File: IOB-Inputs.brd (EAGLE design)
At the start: 20.3 x 50.8 mm, 34 parts, among them J1 RJ12/6, Q0 P-FET, Q1 P-FET, Q2 P-FET, Q3 P-FET

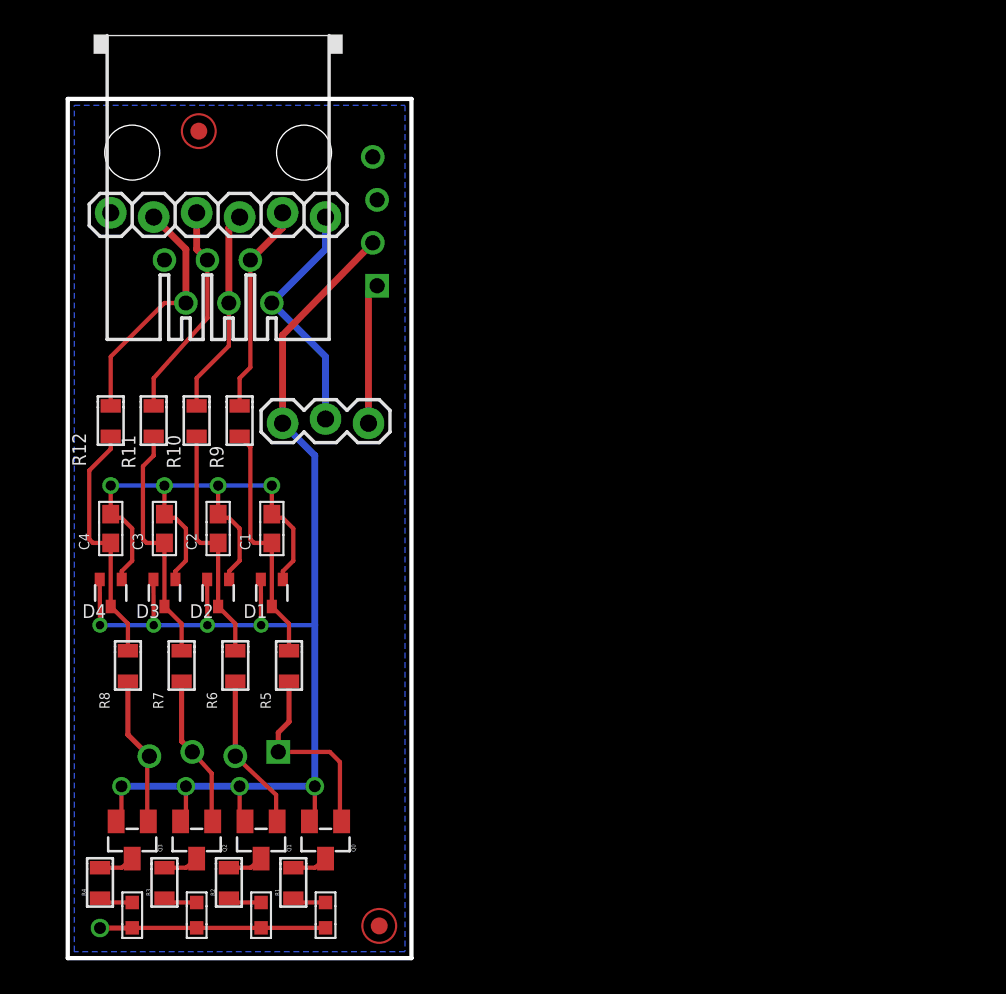
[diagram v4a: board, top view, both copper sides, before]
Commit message: new IOB design
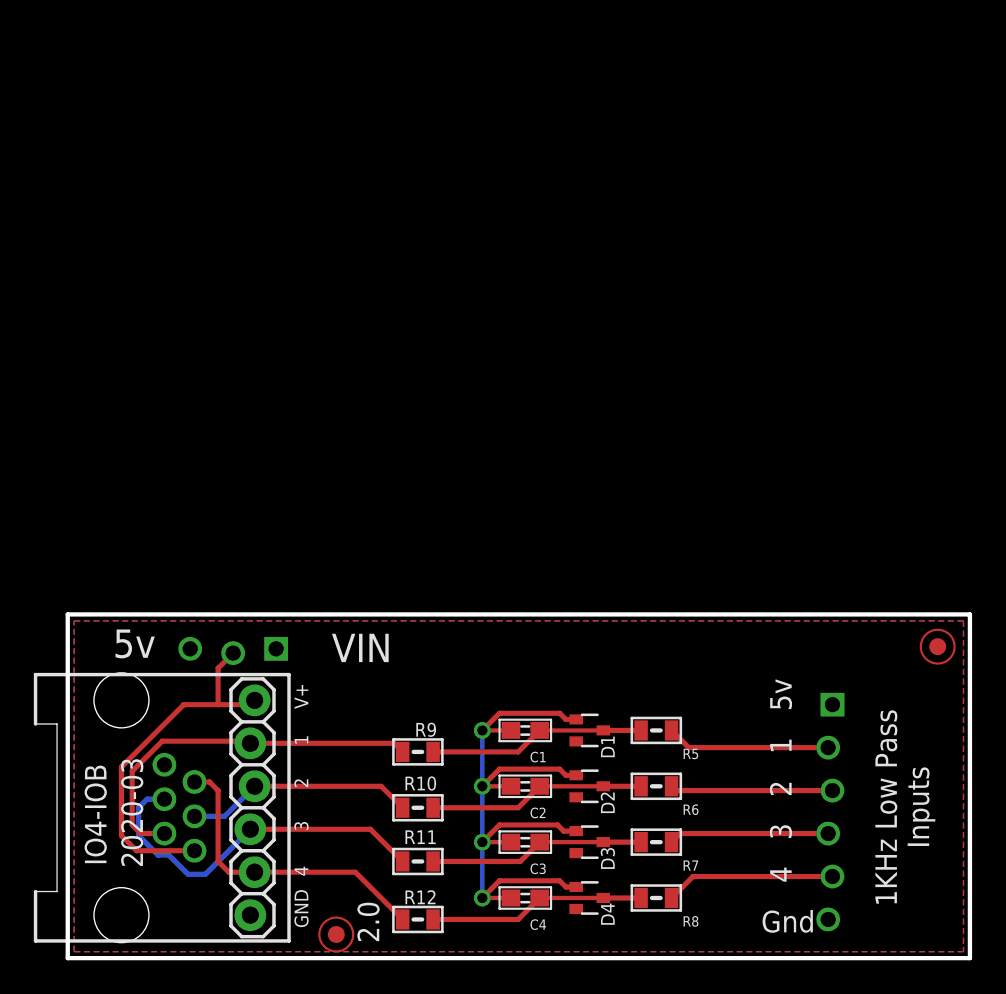
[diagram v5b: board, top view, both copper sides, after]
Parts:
- removed CON1: (no value), SPCoast:1X06_LOCK
- removed LED1, LED2, LED3, LED4: Y, SPCoast:0603-LED
- removed Q0, Q1, Q2, Q3: P-FET, SPCoast:SOT23
- removed R1, R2, R3, R4: 2K0, SPCoast:0805-RES
- removed VIN: (no value), SPCoast:1X03
- J1: device SPCoast:RJ25-PANEL -> SPCoast:RJ24-INVERTED-PINS
- moved IOB 50.8 mm to (0.00, 0.00), turned to 0 degrees
- moved FID1 48.2 mm to (15.9, 1.40), turned to 0 degrees
- moved J1 38.8 mm to (6.99, 8.89), turned to 90 degrees
- moved FID2 36.9 mm to (51.4, 18.4), turned to 0 degrees
- moved R12 34.6 mm to (20.7, 2.29), turned to 180 degrees
- moved R8 34.1 mm to (34.8, 3.56), turned to 180 degrees
- moved D4 33.6 mm to (30.9, 3.56), turned to 270 degrees
- moved C4 32.8 mm to (27.1, 3.56), turned to 180 degrees
- moved R11 30.4 mm to (20.7, 5.71), turned to 180 degrees
- moved R7 29.9 mm to (34.8, 6.86), turned to 180 degrees
- moved D3 29.1 mm to (30.9, 6.86), turned to 270 degrees
- moved C3 28.3 mm to (27.1, 6.86), turned to 180 degrees
- moved R10 26.3 mm to (20.7, 8.89), turned to 180 degrees
- moved R6 25.9 mm to (34.8, 10.2), turned to 180 degrees
- moved D2 24.8 mm to (30.9, 10.2), turned to 270 degrees
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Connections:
- removed net N$1: CON1.1, J1.1, VIN.2
- removed net N$11: Q0.3, R1.2
- removed net N$2: LED1.A, R1.1
- removed net N$3: LED2.A, R2.1
- removed net N$30: Q1.3, R2.2
- removed net N$31: Q2.3, R3.2
- removed net N$32: Q3.3, R4.2
- removed net N$4: LED3.A, R3.1
- removed net N$5: LED4.A, R4.1
- new net VOUT: IOB.VOUT, J1.1, J1.1@1
- net !IO1: now also J1.2@1; no longer CON1.2
- net !IO2: now also J1.3@1; no longer CON1.3
- net !IO3: now also J1.4@1; no longer CON1.4
- net !IO4: now also J1.5@1; no longer CON1.5
- net GND: now also IOB.G@3, J1.6@1; no longer CON1.6, IOB.G@1, IOB.G@2, LED1.C, LED2.C, LED3.C, LED4.C
- net P1: no longer Q0.1
- net P2: no longer Q1.1
- net P3: no longer Q2.1
- net P4: no longer Q3.1
- net VCC: now also IOB.V5@1; no longer Q0.2, Q1.2, Q2.2, Q3.2, VIN.1
- net VCCIO: no longer VIN.3
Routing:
- net VCC: track 79.2 -> 0.00 mm, vias 8 -> 0
- net VOUT: track 0.00 -> 21.7 mm
- net N$1: track 14.6 -> 0.00 mm
- net !IO1: track 12.5 -> 22.3 mm
- net !IO3: track 12.9 -> 21.8 mm
- net VCCIO: track 8.38 -> 0.00 mm
- net GND: track 49.2 -> 41.2 mm, vias 5 -> 4
- net !IO4: track 14.5 -> 18.1 mm
- net P1: track 12.0 -> 9.68 mm
- net N$31: track 2.11 -> 0.00 mm
- net N$32: track 2.11 -> 0.00 mm
- net N$30: track 2.11 -> 0.00 mm
- net N$11: track 2.11 -> 0.00 mm
- net N$4: track 2.01 -> 0.00 mm
- net N$5: track 2.01 -> 0.00 mm
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- added copper zone on layer 1, net VCC
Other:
- board size 20.3 x 50.8 mm -> 53.3 x 20.3 mm
- board text added: "1KHz Low Pass"
- board text added: "2.0"
- board text added: "2020-03"
- board text removed: "1"
- board text removed: "1.4"
- board text removed: "2"
- board text removed: "3"
- board text removed: "4"
- board text removed: "5v"
- board text removed: "9v"
- board text removed: "IO4 Power"
- board text removed: "IOB to IO4 Interface"
- board text removed: "Made in the PCR, Coast Div, NMRA"
- board text removed: "Model Railroading is Fun!"
- board text removed: "Q0"
- board text removed: "Q1"
- board text removed: "Q2"
- board text removed: "Q3"
- board text removed: "R1"
- board text removed: "R2"
- board text removed: "R3"
- board text removed: "R4"

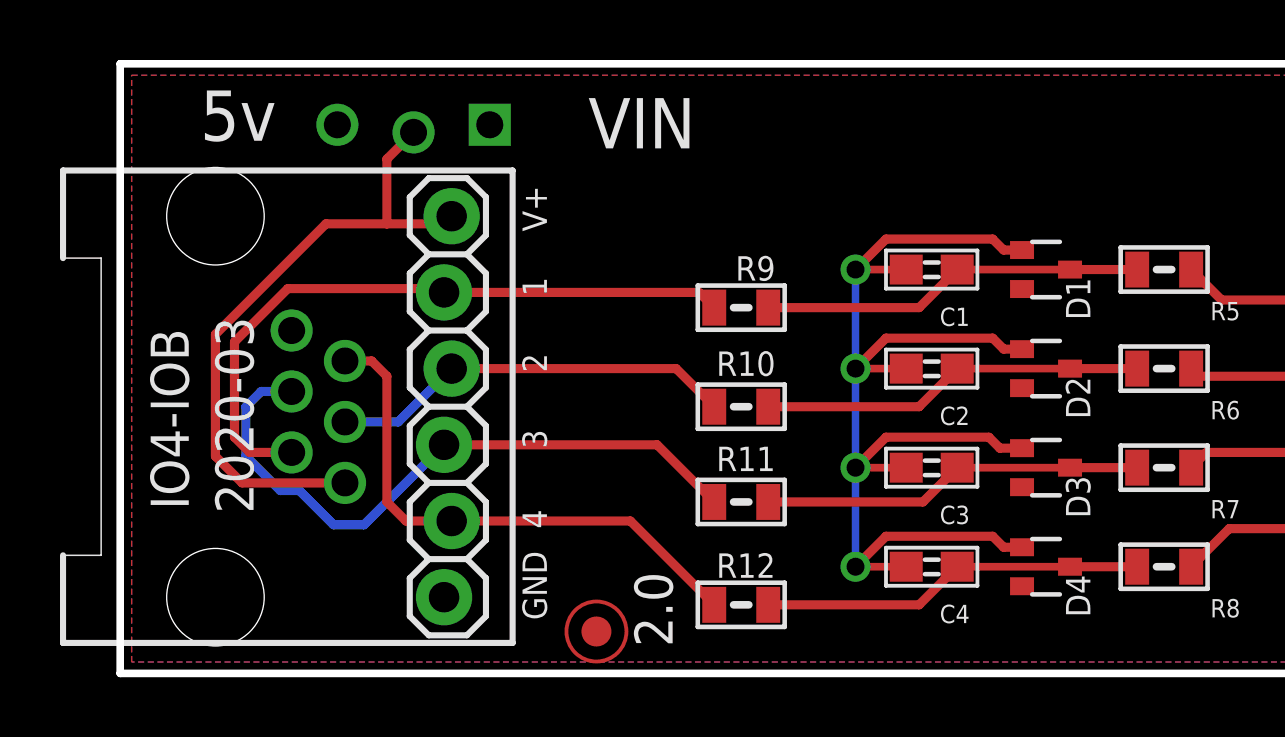
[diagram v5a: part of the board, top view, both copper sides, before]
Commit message: fixed SPCoast.lbr diode orientation
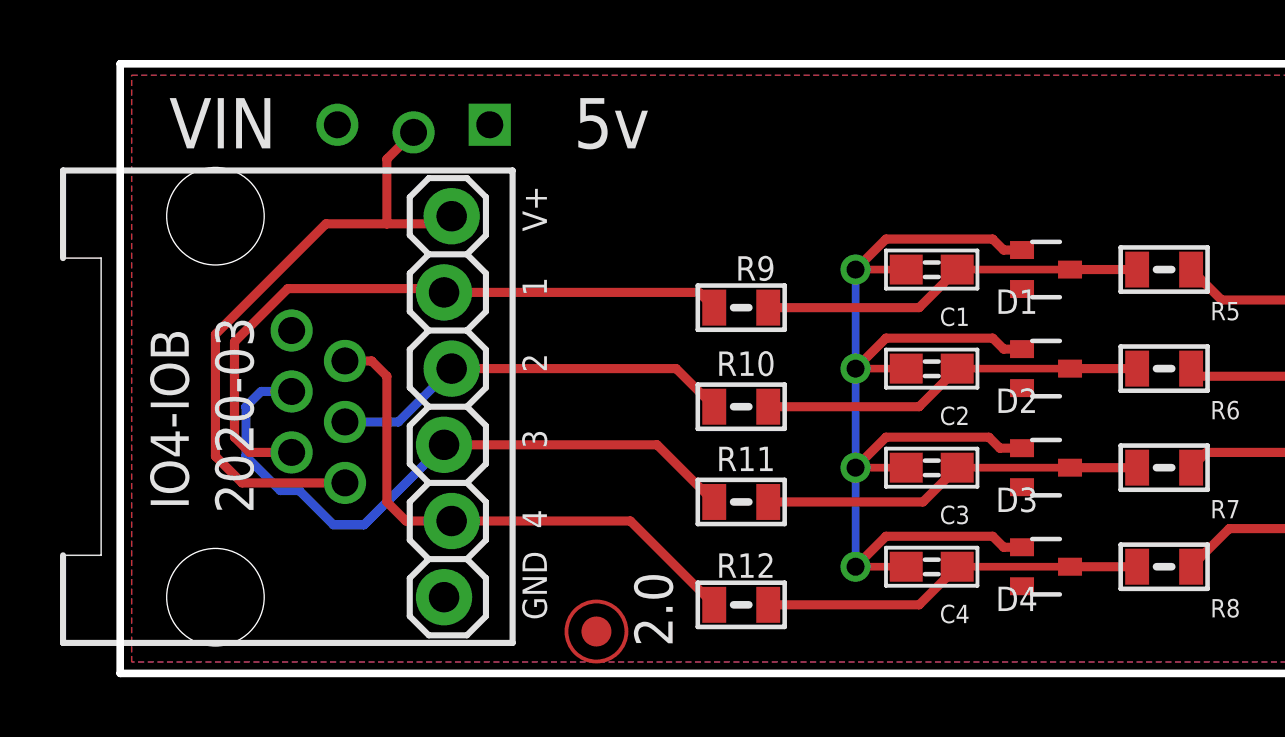
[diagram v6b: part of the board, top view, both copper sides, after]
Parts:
- turned D1 to 180 degrees
- turned D2 to 180 degrees
- turned D3 to 180 degrees
- turned D4 to 180 degrees

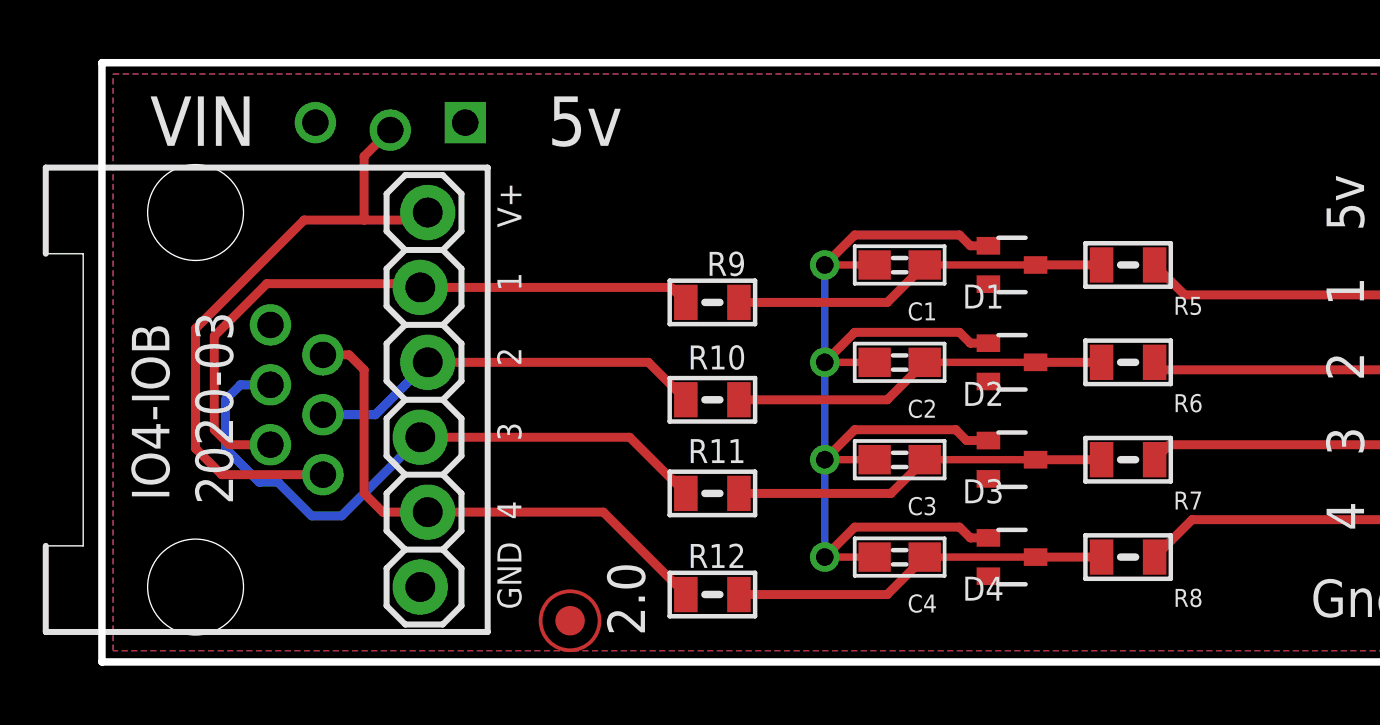
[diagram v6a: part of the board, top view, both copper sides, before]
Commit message: Replaced too small BAT54S SOT23R footprint with SOT23
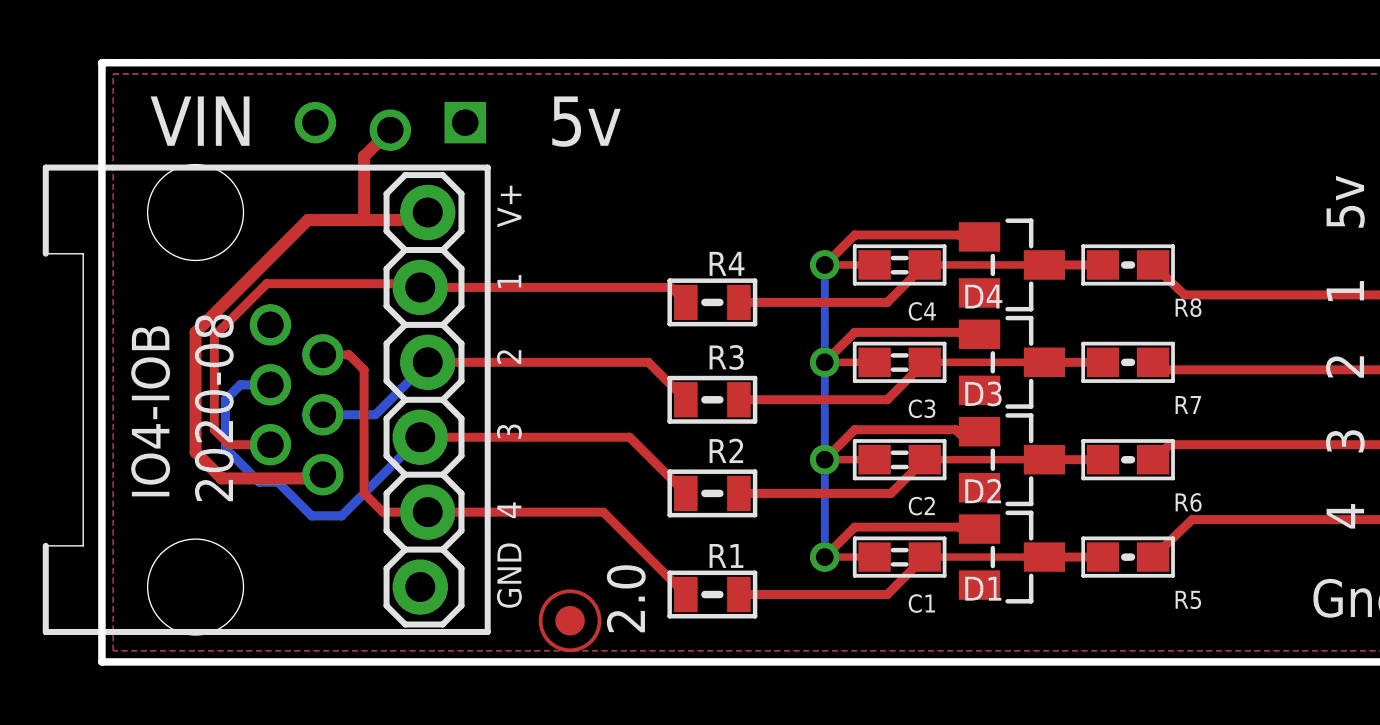
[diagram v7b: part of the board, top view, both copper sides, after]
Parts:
- D1, D2, D3, D4: value (none) -> BAT54S; device SPCoast:SOT323R -> SPCoast:SOT23
- IOB: value CONNECTOR-IO4-IOBBARE -> CONNECTOR-IO4-IOBFULL
- R5, R6, R7, R8: device SPCoast:0805-RES -> SPCoast:0603-RES
- moved C1 9.91 mm to (27.1, 3.56)
- moved C4 9.91 mm to (27.1, 13.5)
- moved D1 9.91 mm to (30.9, 3.56)
- moved D4 9.91 mm to (30.9, 13.5)
- moved R5 9.91 mm to (34.8, 3.56)
- moved R8 9.91 mm to (34.8, 13.5)
- moved C2 3.30 mm to (27.1, 6.86)
- moved C3 3.30 mm to (27.1, 10.2)
- moved D2 3.30 mm to (30.9, 6.86)
- moved D3 3.30 mm to (30.9, 10.2)
- moved R6 3.30 mm to (34.8, 6.86)
- moved R7 3.30 mm to (34.8, 10.2)
- renumbered R10 to R3, R11 to R2, R12 to R1, R9 to R4
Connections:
- net N$10: now also C1.1, D1.3, R5.2; no longer C4.1, D4.2, R8.2
- net N$12: now also C2.1, D2.3, R6.2; no longer C3.1, D3.2, R7.2
- net N$13: now also C3.1, D3.3, R7.2; no longer C2.1, D2.2, R6.2
- net N$14: now also C4.1, D4.3, R8.2; no longer C1.1, D1.2, R5.2
- net P1: now also R8.1; no longer R5.1
- net P2: now also R7.1; no longer R6.1
- net P3: now also R6.1; no longer R7.1
- net P4: now also R5.1; no longer R8.1
- net VCC: now also D1.2, D2.2, D3.2, D4.2; no longer D1.3, D2.3, D3.3, D4.3
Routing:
- net GND: track 41.2 -> 40.4 mm
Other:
- board text added: "2020-08"
- board text added: "Red Headers"
- board text removed: "2020-03"

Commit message: Rev to 2.1 because of Stencil change
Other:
- board text added: "2.1"
- board text removed: "2.0"
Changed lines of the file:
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@@
 <wire x1="0" y1="0" x2="53.34" y2="0" width="0.254" layer="46"/>
 <text x="2.286" y="5.461" size="1.27" layer="21" rot="R90">IO4-IOB</text>
-<text x="18.415" y="0.889" size="1.27" layer="21" rot="R90">2.0</text>
+<text x="18.415" y="0.889" size="1.27" layer="21" rot="R90">2.1</text>
 <text x="50.927" y="6.477" size="1.27" layer="21" rot="R90">Inputs</text>
 <text x="13.843" y="16.764" size="1.27" layer="22" rot="MR270">John Plocher</text>
